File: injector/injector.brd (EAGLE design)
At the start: 68.6 x 53.3 mm, 23 parts, among them IC1 MCP2515-E/SO, IC2 MCP2562, IC3 LM2595NDH

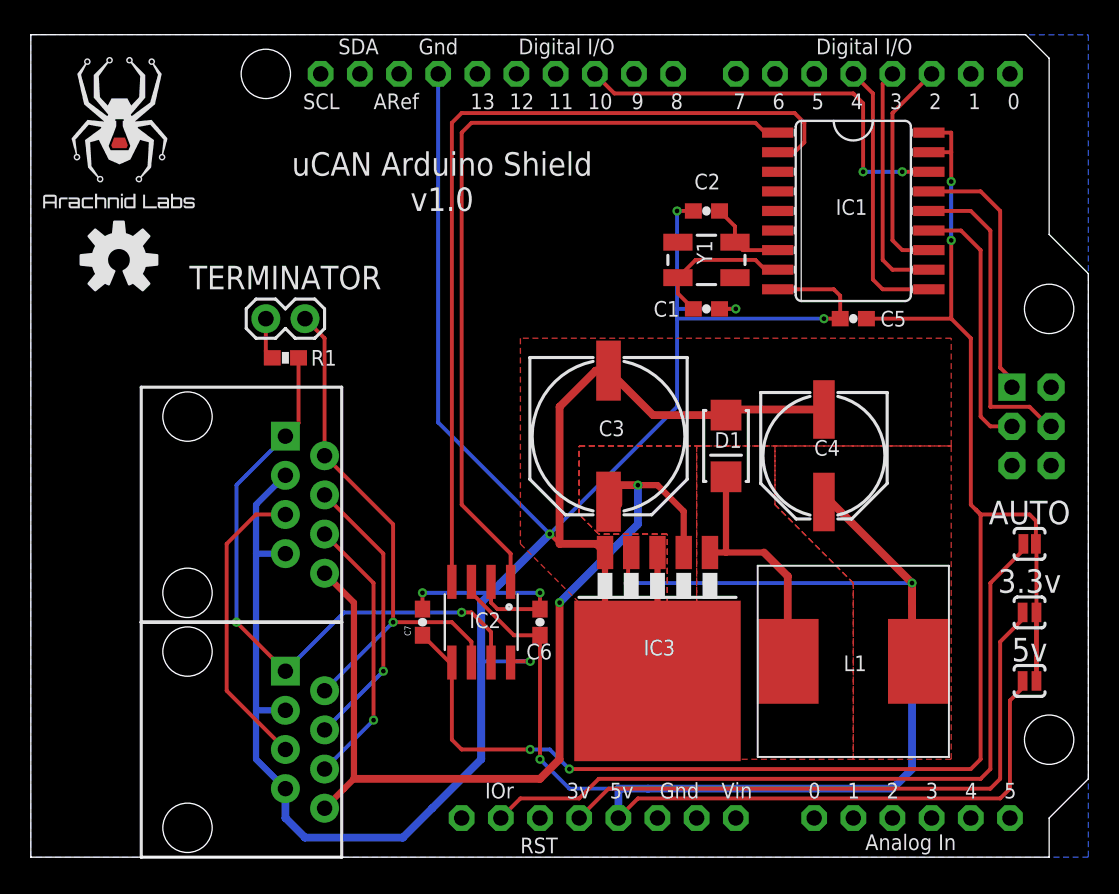
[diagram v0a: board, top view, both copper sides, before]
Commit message: Added power injector board; refactored boards to use MCP2562 instead of MCP2551
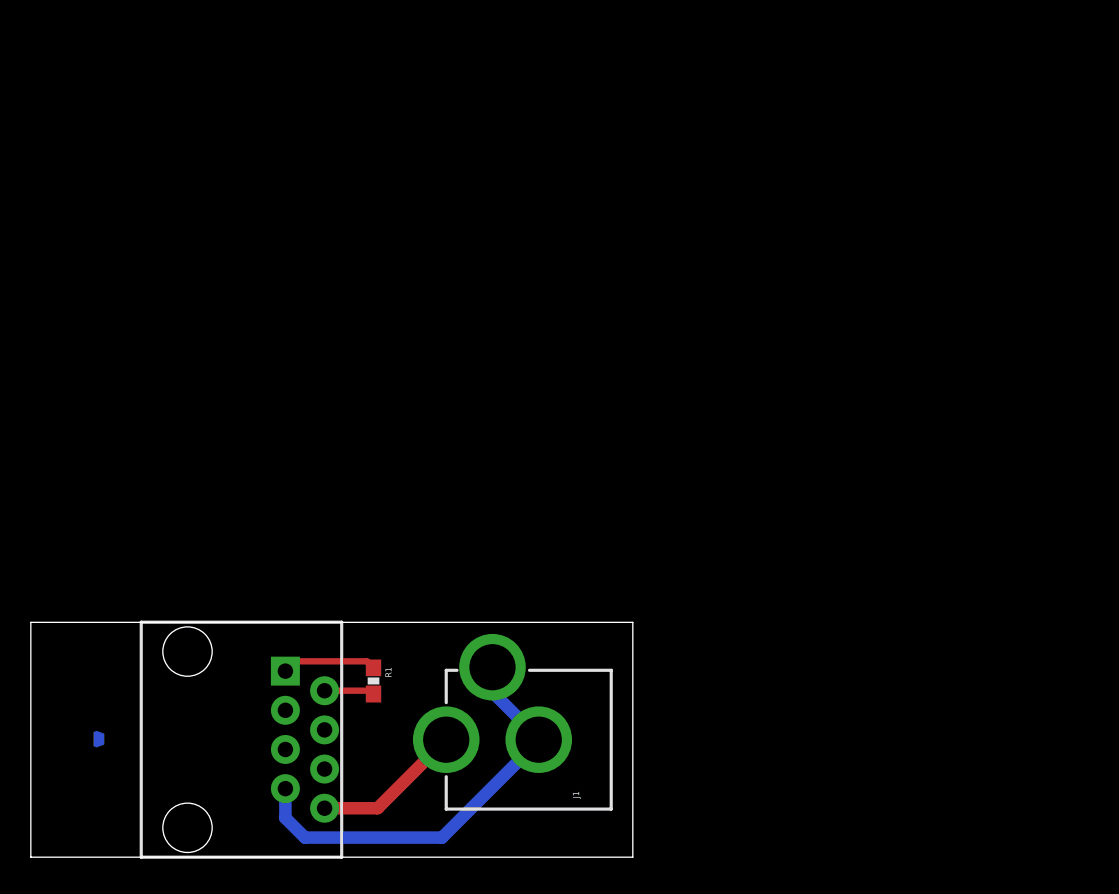
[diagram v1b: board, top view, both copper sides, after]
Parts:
- removed C1, C2: 18p, SparkFun-Capacitors:0603-CAP
- removed C3: (no value), SparkFun-Capacitors:PANASONIC_G
- removed C4: (no value), SparkFun-Capacitors:PANASONIC_E
- removed C5, C6, C7: 0.1u, SparkFun-Passives:0603-CAP
- removed D1: (no value), SparkFun-DiscreteSemi:SMA-DIODE_ALT
- removed IC1: MCP2515-E/SO, mcp2515:SO18L
- removed IC2: MCP2562, nickparts:SO08
- removed IC3: LM2595NDH, nickparts:TO263-5
- removed JP1: (no value), SparkFun-Passives:1X02
- removed L1: MSS1260, nickparts:MSS1260
- removed SJ1: SOLDERJUMPERNC2, SparkFun-Passives:SJ_2S-NOTRACE
- removed SJ2, SJ3: SOLDERJUMPERNO, SparkFun-Passives:SJ_2S-NO
- removed U$3: RJ45-8PTH, SparkFun-Connectors:RJ45-8
- removed U$4: (no value), nickparts:ARACHNID_LABS_LOGO_SM
- removed U$5: (no value), SparkFun-Aesthetics:OSHW-LOGO-M
- removed Y1: (no value), SparkFun-FreqCtrl:CRYSTAL-SMD-5X3
- added J1: POWER_JACKPTH, SparkFun-Connectors:POWER_JACK_PTH
- U$1: value ARDUINO_R3_ICSP -> RJ45-8PTH; device adafruit:ARDUINOR3_ICSP -> SparkFun-Connectors:RJ45-8
- U$2: value RJ45-8PTH -> (none); device SparkFun-Connectors:RJ45-8 -> nickparts:ARACHNID_LABS_LOGO_SM
- moved R1 21.7 mm to (22.2, 11.4), turned to 270 degrees
- moved U$2 16.1 mm to (5.08, 7.62), flipped to the bottom, turned to 90 degrees
- moved U$1 12.7 mm to (10.2, 7.62), turned to 270 degrees
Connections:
- removed net +3V3: SJ3.1, U$1.3V
- removed net +5V: C4.+, C6.1, IC2.3, IC3.4, L1.P$2, SJ2.1, U$1.5V
- removed net 5V: U$1.+5V
- removed net CANH: IC2.7, R1.2, U$2.1, U$3.1
- removed net CANL: IC2.6, JP1.1, U$2.2, U$3.2
- removed net CAN_INT: IC1.12, U$1.D2
- removed net GND: C1.2, C2.2, C3.-, C4.-, C5.2, C6.2, C7.2, D1.A, IC1.9, IC2.2, IC2.8, IC3.3, IC3.5, IC3.6, U$1.GND, U$2.3, U$2.7, U$3.3, U$3.7
- removed net GND$1: U$1.GND$1
- removed net GND$2: U$1.GND$2
- removed net N$10: U$2.4, U$3.4
- removed net N$11: U$2.5, U$3.5
- removed net N$12: U$2.6, U$3.6
- removed net N$5: C2.1, IC1.7, Y1.1
- removed net N$6: D1.C, IC3.1, L1.P$1
- removed net N$7: JP1.2, R1.1
- removed net RX0_BF: IC1.11, U$1.D3
- removed net RX1_BF: IC1.10, U$1.D4
- removed net SPI0_CE0: IC1.16, U$1.D10
- removed net SPI0_MISO: IC1.15, U$1.MISO
- removed net SPI0_MOSI: IC1.14, U$1.MOSI
- removed net SPI0_SCLK: IC1.13, U$1.SCK
- removed net TXCAN: IC1.1, IC2.1
- removed net V+: C5.1, C7.1, IC1.17, IC1.18, IC2.5, SJ1.2, SJ2.2, SJ3.2
- removed net VCC: C3.+, IC3.2, U$2.8, U$3.8
- removed net VCCIO: SJ1.1, U$1.IOREF
- removed net VIN: U$1.VIN
- new net N$2: R1.2, U$1.2
- new net N$3: J1.PWR, U$1.8
- net N$1: now also R1.1, U$1.1; no longer IC1.2, IC2.4
- net N$4: now also J1.GND, J1.GNDBREAK, U$1.7; no longer C1.1, IC1.8, Y1.3
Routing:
- net GND: track 210.0 -> 0.00 mm, vias 7 -> 0
- net +5V: track 122.2 -> 0.00 mm, vias 3 -> 0
- net V+: track 111.9 -> 0.00 mm, vias 4 -> 0
- net VCC: track 62.2 -> 0.00 mm, vias 2 -> 0
- net TXCAN: track 51.5 -> 0.00 mm
- net N$1: track 56.8 -> 6.15 mm
- net VCCIO: track 48.6 -> 0.00 mm
- net CANH: track 40.7 -> 0.00 mm, vias 2 -> 0
- net +3V3: track 39.8 -> 0.00 mm
- net CANL: track 35.3 -> 0.00 mm, vias 1 -> 0
- net SPI0_CE0: track 26.9 -> 0.00 mm, vias 2 -> 0
- net SPI0_MOSI: track 20.4 -> 0.00 mm
- net N$11: track 19.5 -> 0.00 mm
- net N$10: track 18.4 -> 0.00 mm, vias 1 -> 0
- net N$4: track 9.65 -> 27.7 mm
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- removed copper zone on layer 1, net +5V
- removed copper zone on layer 1, net GND
- removed copper zone on layer 16, net GND
- removed copper zone on layer 1, net N$6
- removed copper zone on layer 1, net VCC
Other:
- board size 68.6 x 53.3 mm -> 39 x 15.2 mm
- board text added: "uCAN Power Injector v1.0"
- board text removed: "3.3v"
- board text removed: "5v"
- board text removed: "AUTO"
- board text removed: "TERMINATOR"
- board text removed: "uCAN Arduino Shield v1.0"

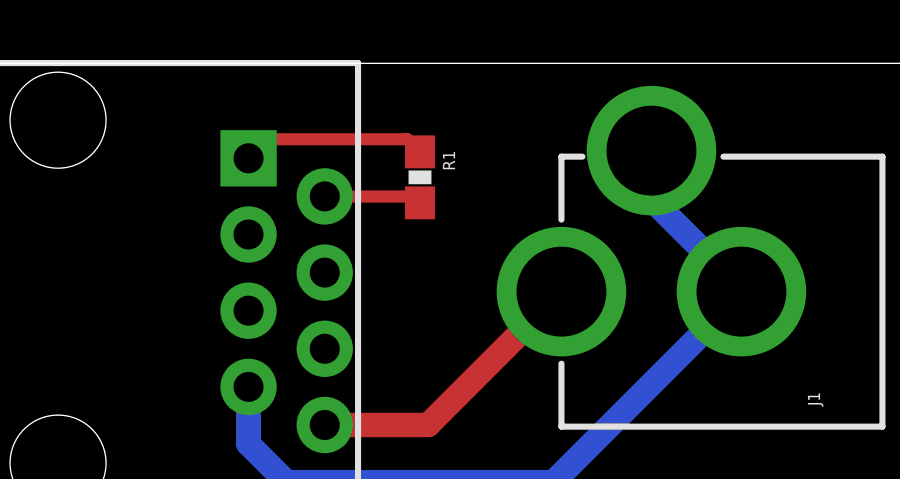
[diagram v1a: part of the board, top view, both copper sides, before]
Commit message: Modify injector for split termination
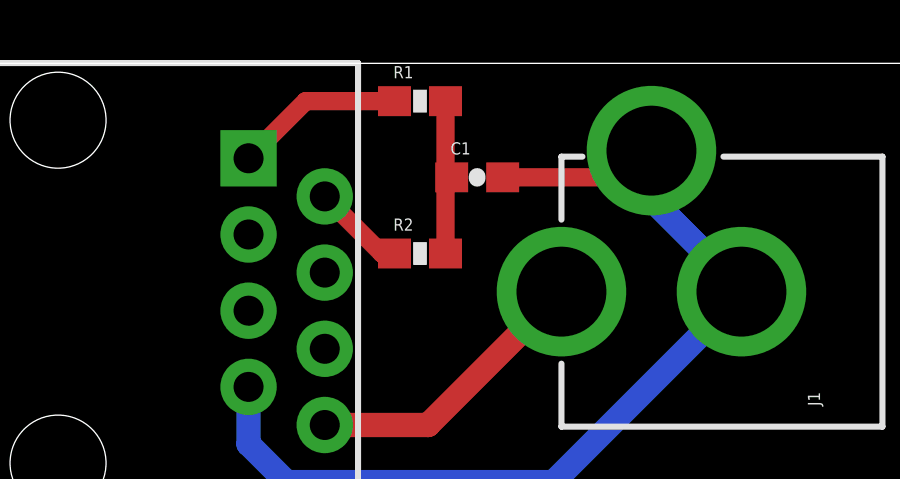
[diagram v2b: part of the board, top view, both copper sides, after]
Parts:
- added C1: (no value), SparkFun-Capacitors:0603-CAP
- added R2: 60, SparkFun-Passives:0603-RES
- R1: value 120 -> 60
- moved R1 2.54 mm to (22.2, 14.0), turned to 0 degrees
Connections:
- new net N$5: C1.1, R1.2, R2.2
- net N$2: now also R2.1; no longer R1.2
- net N$4: now also C1.2
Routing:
- net N$4: track 27.7 -> 33.0 mm
- net N$5: track 0.00 -> 5.25 mm
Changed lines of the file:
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@@
 <elements>
 <element name="U$1" library="SparkFun-Connectors" package="RJ45-8" value="RJ45-8PTH" x="10.16" y="7.62" rot="R270"/>
-<element name="R1" library="SparkFun-Passives" package="0603-RES" value="120" x="22.225" y="11.43" rot="R270"/>
+<element name="R1" library="SparkFun-Passives" package="0603-RES" value="60" x="22.225" y="13.97"/>
 <element name="J1" library="SparkFun-Connectors" package="POWER_JACK_PTH" value="POWER_JACKPTH" x="40.64" y="7.62" rot="R90"/>
 <element name="U$2" library="nickparts" package="ARACHNID_LABS_LOGO_SM" value="" x="5.08" y="7.62" rot="MR90"/>
+<element name="R2" library="SparkFun-Passives" package="0603-RES" value="60" x="22.225" y="8.89"/>
+<element name="C1" library="SparkFun-Capacitors" package="0603-CAP" value="" x="24.13" y="11.43"/>
 </elements>
 <signals>
-<signal name="N$1">
-<contactref element="U$1" pad="1"/>
-<contactref element="R1" pad="1"/>
-<wire x1="16.51" y1="12.065" x2="17.145" y2="12.7" width="0.4064" layer="1"/>
-<wire x1="17.145" y1="12.7" x2="21.805" y2="12.7" width="0.4064" layer="1"/>
-<wire x1="21.805" y1="12.7" x2="22.225" y2="12.28" width="0.4064" layer="1"/>
-</signal>
-<signal name="N$2">
-<contactref element="R1" pad="2"/>
-<contactref element="U$1" pad="2"/>
-<wire x1="19.05" y1="10.795" x2="22.01" y2="10.795" width="0.4064" layer="1"/>
-<wire x1="22.01" y1="10.795" x2="22.225" y2="10.58" width="0.4064" layer="1"/>
-</signal>
 <signal name="N$3">
 <contactref element="U$1" pad="8"/>
@@
 <wire x1="29.94" y1="10.7" x2="33.02" y2="7.62" width="0.8128" layer="16"/>
 <wire x1="33.02" y1="7.62" x2="32.94" y2="7.62" width="0.8128" layer="16"/>
+<contactref element="C1" pad="2"/>
+<wire x1="24.98" y1="11.43" x2="29.05" y2="11.43" width="0.6096" layer="1"/>
+<wire x1="29.05" y1="11.43" x2="29.94" y2="12.32" width="0.6096" layer="1"/>
+</signal>
+<signal name="N$1">
+<contactref element="U$1" pad="1"/>
+<contactref element="R1" pad="1"/>
+<wire x1="21.375" y1="13.97" x2="18.415" y2="13.97" width="0.6096" layer="1"/>
+<wire x1="18.415" y1="13.97" x2="16.51" y2="12.065" width="0.6096" layer="1"/>
+</signal>
+<signal name="N$2">
+<contactref element="U$1" pad="2"/>
+<contactref element="R2" pad="1"/>
+<wire x1="21.375" y1="8.89" x2="20.955" y2="8.89" width="0.6096" layer="1"/>
+<wire x1="20.955" y1="8.89" x2="19.05" y2="10.795" width="0.6096" layer="1"/>
+</signal>
+<signal name="N$5">
+<contactref element="R2" pad="2"/>
+<contactref element="C1" pad="1"/>
+<contactref element="R1" pad="2"/>
+<wire x1="23.075" y1="13.97" x2="23.075" y2="11.635" width="0.6096" layer="1"/>
+<wire x1="23.075" y1="11.635" x2="23.28" y2="11.43" width="0.6096" layer="1"/>
+<wire x1="23.075" y1="8.89" x2="23.075" y2="11.225" width="0.6096" layer="1"/>
+<wire x1="23.075" y1="11.225" x2="23.28" y2="11.43" width="0.6096" layer="1"/>
 </signal>
 </signals>

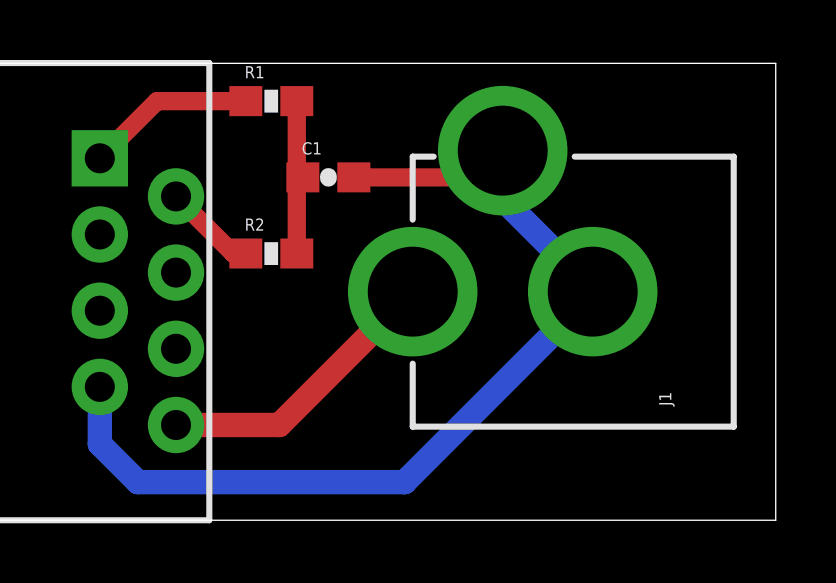
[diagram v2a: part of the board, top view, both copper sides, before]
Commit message: Added TVS diodes, fixed silkscreen issues
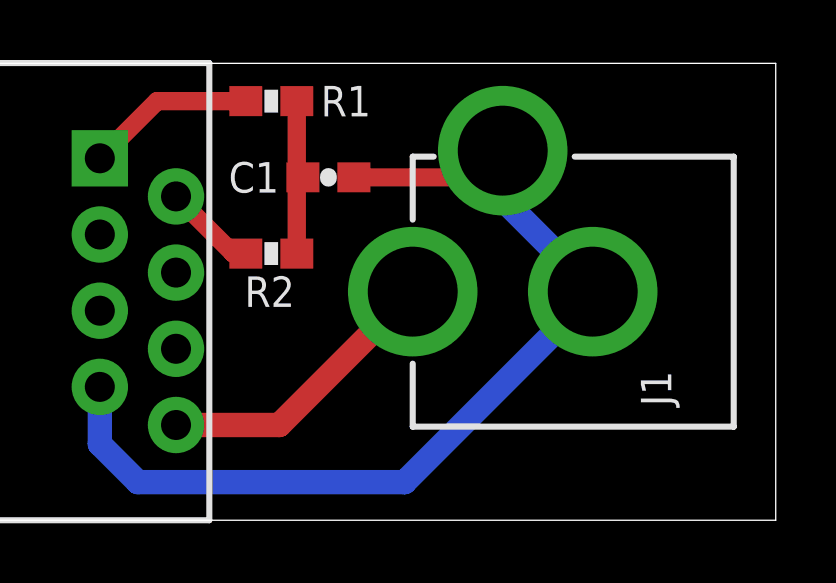
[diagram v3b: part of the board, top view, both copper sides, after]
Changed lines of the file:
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@@
 <elements>
 <element name="U$1" library="SparkFun-Connectors" package="RJ45-8" value="RJ45-8PTH" x="10.16" y="7.62" rot="R270"/>
-<element name="R1" library="SparkFun-Passives" package="0603-RES" value="60" x="22.225" y="13.97"/>
-<element name="J1" library="SparkFun-Connectors" package="POWER_JACK_PTH" value="POWER_JACKPTH" x="40.64" y="7.62" rot="R90"/>
+<element name="R1" library="SparkFun-Passives" package="0603-RES" value="60" x="22.225" y="13.97" smashed="yes">
+<attribute name="NAME" x="23.876" y="13.462" size="1.016" layer="25" font="vector" ratio="15"/>
+</element>
+<element name="J1" library="SparkFun-Connectors" package="POWER_JACK_PTH" value="POWER_JACKPTH" x="40.64" y="7.62" smashed="yes" rot="R90">
+<attribute name="NAME" x="35.56" y="3.81" size="1.016" layer="25" font="vector" ratio="15" rot="R90"/>
+</element>
 <element name="U$2" library="nickparts" package="ARACHNID_LABS_LOGO_SM" value="" x="5.08" y="7.62" rot="MR90"/>
-<element name="R2" library="SparkFun-Passives" package="0603-RES" value="60" x="22.225" y="8.89"/>
-<element name="C1" library="SparkFun-Capacitors" package="0603-CAP" value="" x="24.13" y="11.43"/>
+<element name="R2" library="SparkFun-Passives" package="0603-RES" value="60" x="22.225" y="8.89" smashed="yes">
+<attribute name="NAME" x="21.336" y="7.112" size="1.016" layer="25" font="vector" ratio="15"/>
+</element>
+<element name="C1" library="SparkFun-Capacitors" package="0603-CAP" value="" x="24.13" y="11.43" smashed="yes">
+<attribute name="NAME" x="22.479" y="11.938" size="1.016" layer="25" font="vector" ratio="15" rot="R180"/>
+<attribute name="VALUE" x="23.114" y="10.287" size="0.4064" layer="27" font="vector"/>
+</element>
 </elements>
 <signals>
